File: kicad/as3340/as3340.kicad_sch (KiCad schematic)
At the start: 45 parts, among them J1 Conn_01x01, J3 Conn_02x20_Odd_Even, U1 TL074, U11 LM393, U12 TL074, U15 M24C02-WMN, U2 TL074, U4 PS508, U5 MAX333A, U6 AS3360, U7 PCA9555D, U8 DG442CY+, U9 DG442CY+

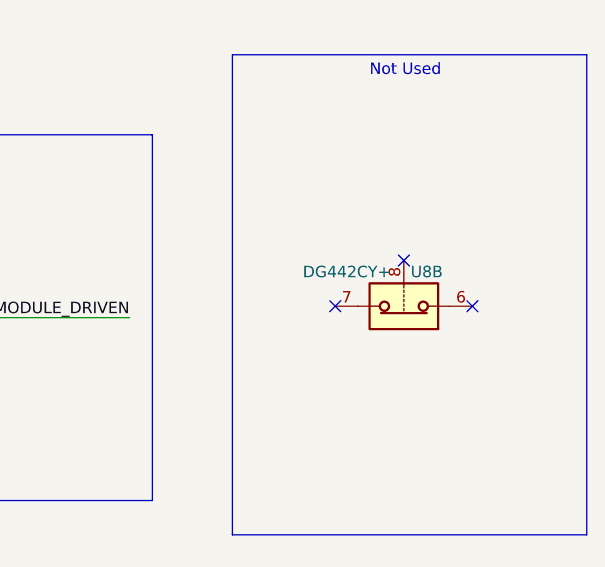
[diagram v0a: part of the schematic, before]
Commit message: tie unused switch to ground
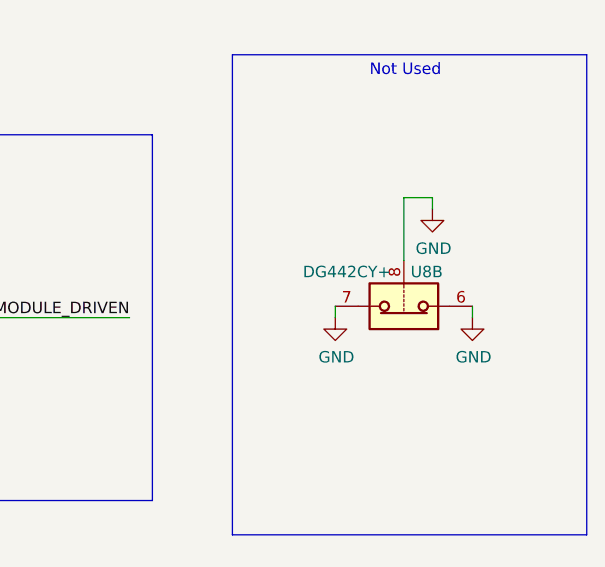
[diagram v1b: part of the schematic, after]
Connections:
- net GND: now also U8.6, U8.7, U8.8
- no-connect marks 12 -> 9
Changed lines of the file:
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@@
   (junction (at 323.85 209.55) (diameter 0) (color 0 0 0 0)
   )
-  (no_connect (at 398.78 203.2))
   (no_connect (at 54.61 77.47))
   (no_connect (at 172.72 54.61))
@@
   (no_connect (at 54.61 34.29))
   (no_connect (at 54.61 72.39))
-  (no_connect (at 406.4 208.28))
-  (no_connect (at 391.16 208.28))
   (no_connect (at 54.61 74.93))
   (wire (pts (xy 24.13 234.95) (xy 24.13 237.49))
@@
     (stroke (width 0) (type default) (color 0 0 0 0))
   )
+  (wire (pts (xy 406.4 208.28) (xy 406.4 209.55))
+    (stroke (width 0) (type default) (color 0 0 0 0))
+  )
   (polyline (pts (xy 293.37 234.95) (xy 293.37 262.89))
     (stroke (width 0) (type default) (color 0 0 0 0))
@@
     (stroke (width 0) (type default) (color 0 0 0 0))
   )
+  (wire (pts (xy 401.955 197.485) (xy 401.955 196.215))
+    (stroke (width 0) (type default) (color 0 0 0 0))
+  )
   (polyline (pts (xy 257.81 262.89) (xy 257.81 234.95))
     (stroke (width 0) (type default) (color 0 0 0 0))
@@
     (stroke (width 0) (type default) (color 0 0 0 0))
   )
+  (wire (pts (xy 391.16 208.28) (xy 391.16 209.55))
+    (stroke (width 0) (type default) (color 0 0 0 0))
+  )
   (wire (pts (xy 109.22 52.07) (xy 109.22 54.61))
     (stroke (width 0) (type default) (color 0 0 0 0))
@@
     (stroke (width 0) (type default) (color 0 0 0 0))
   )
+  (wire (pts (xy 401.955 196.215) (xy 398.78 196.215))
+    (stroke (width 0) (type default) (color 0 0 0 0))
+  )
   (wire (pts (xy 109.22 34.29) (xy 109.22 39.37))
     (stroke (width 0) (type default) (color 0 0 0 0))
@@
     (stroke (width 0) (type default) (color 0 0 0 0))
   )
+  (wire (pts (xy 398.78 196.215) (xy 398.78 203.2))
+    (stroke (width 0) (type default) (color 0 0 0 0))
+  )
   (wire (pts (xy 335.28 52.07) (xy 323.85 52.07))
     (stroke (width 0) (type default) (color 0 0 0 0))
@@
     (pin "1")
   )
+  (symbol (lib_id "power:GND") (at 391.16 209.55 0) (unit 1)
+    (in_bom yes) (on_board yes)
+    (property "Reference" "#PWR071" (id 0) (at 391.16 215.9 0)
+      (effects (font (size 1.27 1.27)) hide)
+    )
+    (property "Value" "GND" (id 1) (at 391.287 213.9442 0))
+    (property "Footprint" "" (id 2) (at 391.16 209.55 0)
+      (effects (font (size 1.27 1.27)) hide)
+    )
+    (property "Datasheet" "" (id 3) (at 391.16 209.55 0)
+      (effects (font (size 1.27 1.27)) hide)
+    )
+    (pin "1")
+  )
+  (symbol (lib_id "power:GND") (at 406.4 209.55 0) (unit 1)
+    (in_bom yes) (on_board yes)
+    (property "Reference" "#PWR074" (id 0) (at 406.4 215.9 0)
+      (effects (font (size 1.27 1.27)) hide)
+    )
+    (property "Value" "GND" (id 1) (at 406.527 213.9442 0))
+    (property "Footprint" "" (id 2) (at 406.4 209.55 0)
+      (effects (font (size 1.27 1.27)) hide)
+    )
+    (property "Datasheet" "" (id 3) (at 406.4 209.55 0)
+      (effects (font (size 1.27 1.27)) hide)
+    )
+    (pin "1")
+  )
   (symbol (lib_id "Connector_Generic:Conn_01x01") (at 391.795 28.575 90) (unit 1)
     (in_bom yes) (on_board yes) (fields_autoplaced)
@@
     (pin "1")
   )
+  (symbol (lib_id "power:GND") (at 401.955 197.485 0) (unit 1)
+    (in_bom yes) (on_board yes)
+    (property "Reference" "#PWR072" (id 0) (at 401.955 203.835 0)
+      (effects (font (size 1.27 1.27)) hide)
+    )
+    (property "Value" "GND" (id 1) (at 402.082 201.8792 0))
+    (property "Footprint" "" (id 2) (at 401.955 197.485 0)
+      (effects (font (size 1.27 1.27)) hide)
+    )
+    (property "Datasheet" "" (id 3) (at 401.955 197.485 0)
+      (effects (font (size 1.27 1.27)) hide)
+    )
+    (pin "1")
+  )
   (sheet (at 162.56 124.46) (size 49.53 45.72) (fields_autoplaced)
     (stroke (width 0) (type solid) (color 0 0 0 0))
@@
       (reference "#PWR070") (unit 1) (value "GND") (footprint "")
     )
+    (path "/2b8704e2-aa1f-40c9-82c8-93dd49fc38ee"
+      (reference "#PWR071") (unit 1) (value "GND") (footprint "")
+    )
+    (path "/ffd638dd-eb53-4da1-84f0-6a181aff412d"
+      (reference "#PWR072") (unit 1) (value "GND") (footprint "")
+    )
     (path "/00000000-0000-0000-0000-000064b423a8"
       (reference "#PWR073") (unit 1) (value "GND") (footprint "")
     )
+    (path "/2e02bdbd-8922-492a-83ea-736cc68f050d"
+      (reference "#PWR074") (unit 1) (value "GND") (footprint "")
+    )
     (path "/00000000-0000-0000-0000-0000645cbcd1"

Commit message: fixes for BOM
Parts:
- C1, C2, C3, C30, C31, C4: LCSC C14663 -> (none)
- U2: LCSC C504548 -> (none)
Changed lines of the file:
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@@
       (effects (font (size 1.27 1.27)) hide)
     )
-    (property "LCSC" "C504548" (id 4) (at 92.71 232.41 0)
+    (property "LCSC" "" (id 4) (at 92.71 232.41 0)
       (effects (font (size 1.27 1.27)) hide)
     )
@@
       (effects (font (size 1.27 1.27)) hide)
     )
-    (property "LCSC" "C14663" (id 4) (at 24.13 241.3 0)
+    (property "LCSC" "" (id 4) (at 24.13 241.3 0)
       (effects (font (size 1.27 1.27)) hide)
     )
@@
       (effects (font (size 1.27 1.27)) hide)
     )
-    (property "LCSC" "C14663" (id 4) (at 24.13 229.87 0)
+    (property "LCSC" "" (id 4) (at 24.13 229.87 0)
       (effects (font (size 1.27 1.27)) hide)
     )
@@
       (effects (font (size 1.27 1.27)) hide)
     )
-    (property "LCSC" "C14663" (id 4) (at 80.01 240.03 0)
-      (effects (font (size 1.27 1.27)) hide)
-    )
     (property "LCSC Part" "C14663" (id 5) (at 80.01 240.03 0)
       (effects (font (size 1.27 1.27)) hide)
@@
     )
     (property "Datasheet" "~" (id 3) (at 80.01 228.6 0)
-      (effects (font (size 1.27 1.27)) hide)
-    )
-    (property "LCSC" "C14663" (id 4) (at 80.01 228.6 0)
       (effects (font (size 1.27 1.27)) hide)
     )
@@
       (effects (font (size 1.27 1.27)) hide)
     )
-    (property "LCSC" "C14663" (id 4) (at 50.8 242.57 0)
-      (effects (font (size 1.27 1.27)) hide)
-    )
     (property "LCSC Part" "C14663" (id 5) (at 50.8 242.57 0)
       (effects (font (size 1.27 1.27)) hide)
@@
       (effects (font (size 1.27 1.27)) hide)
     )
-    (property "LCSC" "C14663" (id 4) (at 50.8 231.14 0)
-      (effects (font (size 1.27 1.27)) hide)
-    )

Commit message: update title block and add schematic pdf
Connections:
- net CARD2_OUT2: no longer names the net of J3.25 (Pin_25)
- net CARD3_OUT2: no longer names the net of J3.27 (Pin_27)
- net CARD4_OUT2: no longer names the net of J3.30 (Pin_30)
- net CARD5_OUT2: no longer names the net of J3.33 (Pin_33)
- net CARD6_OUT2: no longer names the net of J3.35 (Pin_35)
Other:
- title: Zoxnoxious 3340 Oscillator: Top Level -> Zoxnoxious 3340 Oscillator
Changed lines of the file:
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@@
   (paper "B")
   (title_block
-    (title "Zoxnoxious 3340 Oscillator: Top Level")
-    (rev "0.3")
+    (title "Zoxnoxious 3340 Oscillator")
+    (date "2022-09-07")
+    (rev "0.4")
     (company "Zoxnoxious Engineering")
   )
@@
   (junction (at 323.85 209.55) (diameter 0) (color 0 0 0 0)
   )
-  (no_connect (at 54.61 77.47))
+  (no_connect (at 69.85 74.93))
   (no_connect (at 172.72 54.61))
-  (no_connect (at 54.61 69.85))
   (no_connect (at 97.79 36.83))
   (no_connect (at 199.39 82.55))
-  (no_connect (at 97.79 72.39))
   (no_connect (at 54.61 34.29))
-  (no_connect (at 54.61 72.39))
-  (no_connect (at 54.61 74.93))
+  (no_connect (at 69.85 72.39))
+  (no_connect (at 82.55 67.31))
+  (no_connect (at 69.85 64.77))
+  (no_connect (at 69.85 62.23))
   (wire (pts (xy 24.13 234.95) (xy 24.13 237.49))
     (stroke (width 0) (type default) (color 0 0 0 0))
@@
     (stroke (width 0) (type default) (color 0 0 0 0))
   )
-  (wire (pts (xy 69.85 72.39) (xy 54.61 72.39))
-    (stroke (width 0) (type default) (color 0 0 0 0))
-  )
   (polyline (pts (xy 257.81 234.95) (xy 293.37 234.95))
     (stroke (width 0) (type default) (color 0 0 0 0))
@@
     (stroke (width 0) (type default) (color 0 0 0 0))
   )
-  (wire (pts (xy 69.85 74.93) (xy 54.61 74.93))
-    (stroke (width 0) (type default) (color 0 0 0 0))
-  )
   (wire (pts (xy 227.33 246.38) (xy 227.33 248.92))
     (stroke (width 0) (type default) (color 0 0 0 0))
@@
     (stroke (width 0) (type default) (color 0 0 0 0))
   )
-  (wire (pts (xy 54.61 64.77) (xy 69.85 64.77))
-    (stroke (width 0) (type default) (color 0 0 0 0))
-  )
   (wire (pts (xy 90.17 251.46) (xy 80.01 251.46))
     (stroke (width 0) (type default) (color 0 0 0 0))
@@
     (stroke (width 0) (type default) (color 0 0 0 0))
   )
-  (wire (pts (xy 97.79 67.31) (xy 82.55 67.31))
-    (stroke (width 0) (type default) (color 0 0 0 0))
-  )
   (wire (pts (xy 33.02 139.7) (xy 21.59 139.7))
     (stroke (width 0) (type default) (color 0 0 0 0))
@@
   )
   (wire (pts (xy 120.65 157.48) (xy 123.19 157.48))
-    (stroke (width 0) (type default) (color 0 0 0 0))
-  )
-  (wire (pts (xy 54.61 62.23) (xy 69.85 62.23))
     (stroke (width 0) (type default) (color 0 0 0 0))
   )
@@
     (effects (font (size 1.27 1.27)) (justify left bottom))
   )
-  (label "CARD3_OUT2" (at 68.58 64.77 180)
-    (effects (font (size 1.27 1.27)) (justify right bottom))
-  )
   (label "GPIO_MODULE_DRIVEN" (at 368.3 209.55 180)
     (effects (font (size 1.27 1.27)) (justify right bottom))
@@
     (effects (font (size 1.27 1.27)) (justify left bottom))
   )
-  (label "CARD2_OUT2" (at 57.15 62.23 0)
-    (effects (font (size 1.27 1.27)) (justify left bottom))
-  )
   (label "CARD1_OUT1" (at 289.56 40.64 0)
     (effects (font (size 1.27 1.27)) (justify left bottom))
@@
     (effects (font (size 1.27 1.27)) (justify left bottom))
   )
-  (label "CARD4_OUT2" (at 95.25 67.31 180)
-    (effects (font (size 1.27 1.27)) (justify right bottom))
-  )
   (label "SPI_CLK" (at 21.59 135.89 0)
     (effects (font (size 1.27 1.27)) (justify left bottom))
@@
     (effects (font (size 1.27 1.27)) (justify left bottom))
   )
-  (label "CARD6_OUT2" (at 68.58 74.93 180)
-    (effects (font (size 1.27 1.27)) (justify right bottom))
-  )
   (label "SYNC_POS_CTRL" (at 199.39 62.23 0)
     (effects (font (size 1.27 1.27)) (justify left bottom))
@@
     (effects (font (size 1.27 1.27)) (justify left bottom))
   )
-  (label "CARD5_OUT2" (at 67.31 72.39 180)
-    (effects (font (size 1.27 1.27)) (justify right bottom))
-  )
   (label "CARD5_OUT1" (at 67.31 69.85 180)

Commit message: add 3340 v0.4 gerbers
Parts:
- U1, U12, U2: LCSC Part C12594 -> C6963
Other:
- note added: "TL074: LCSC Part C6963 or C12594 works"
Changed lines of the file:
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@@
+    (effects (font (size 1.27 1.27)) (justify left bottom))
+  )
+  (text "TL074: LCSC Part C6963 or C12594 works" (at 27.94 264.16 0)
     (effects (font (size 1.27 1.27)) (justify left bottom))
   )
@@
       (effects (font (size 1.27 1.27)) hide)
     )
-    (property "LCSC Part" "C12594" (id 5) (at 92.71 232.41 0)
+    (property "LCSC Part" "C6963" (id 5) (at 92.71 232.41 0)
       (effects (font (size 1.27 1.27)) hide)
     )
@@
       (effects (font (size 1.27 1.27)) hide)
     )
-    (property "LCSC Part" "C12594" (id 4) (at 314.96 209.55 0)
+    (property "LCSC Part" "C6963" (id 4) (at 314.96 209.55 0)
       (effects (font (size 1.27 1.27)) hide)
     )
@@
       (effects (font (size 1.27 1.27)) hide)
     )
-    (property "LCSC Part" "C12594" (id 5) (at 36.83 233.68 0)
+    (property "LCSC Part" "C6963" (id 5) (at 36.83 233.68 0)
       (effects (font (size 1.27 1.27)) hide)
     )
@@
       (effects (font (size 1.27 1.27)) hide)
     )
-    (property "LCSC Part" "C12594" (id 5) (at 63.5 234.95 0)
-      (effects (font (size 1.27 1.27)) hide)
-    )
+    (property "LCSC Part" "C6963" (id 5) (at 63.5 234.95 0)
+      (effects (font (size 1.27 1.27)) hide)
+    )

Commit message: as3340 rev0.4 submitted to jlcpcb
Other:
- note added: "GND Test Point"
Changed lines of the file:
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@@
+    (stroke (width 0) (type default) (color 0 0 0 0))
+  )
+  (polyline (pts (xy 407.67 21.59) (xy 407.67 45.72))
     (stroke (width 0) (type default) (color 0 0 0 0))
   )
@@
     (stroke (width 0) (type default) (color 0 0 0 0))
   )
+  (polyline (pts (xy 382.27 21.59) (xy 407.67 21.59))
+    (stroke (width 0) (type default) (color 0 0 0 0))
+  )
   (wire (pts (xy 276.86 30.48) (xy 276.86 35.56))
     (stroke (width 0) (type default) (color 0 0 0 0))
@@
     (stroke (width 0) (type default) (color 0 0 0 0))
   )
+  (polyline (pts (xy 382.27 21.59) (xy 382.27 45.72))
+    (stroke (width 0) (type default) (color 0 0 0 0))
+  )
   (wire (pts (xy 82.55 34.29) (xy 109.22 34.29))
     (stroke (width 0) (type default) (color 0 0 0 0))
@@
   )
   (wire (pts (xy 336.55 204.47) (xy 336.55 209.55))
+    (stroke (width 0) (type default) (color 0 0 0 0))
+  )
+  (polyline (pts (xy 407.67 45.72) (xy 382.27 45.72))
     (stroke (width 0) (type default) (color 0 0 0 0))
   )
@@
     (effects (font (size 1.27 1.27)) (justify left bottom))
   )
+  (text "GND Test Point" (at 386.08 25.4 0)
+    (effects (font (size 1.27 1.27)) (justify left bottom))
+  )

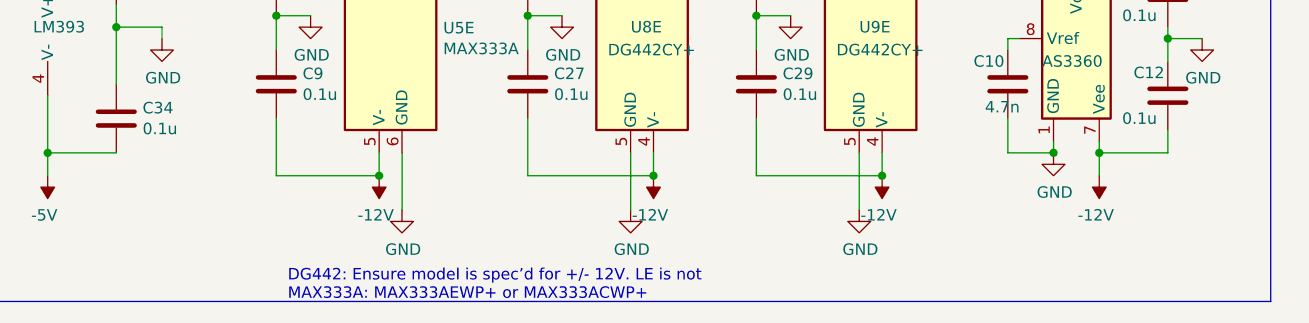
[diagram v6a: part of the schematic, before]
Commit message: update schematic comment on part 333A
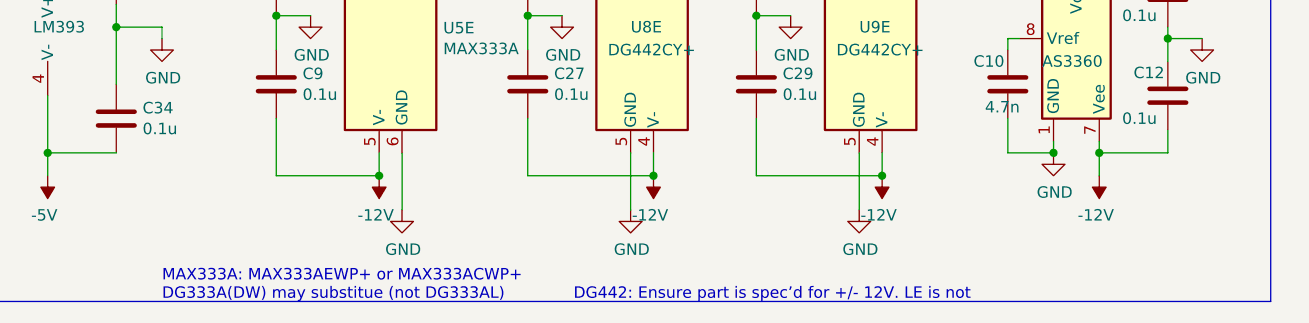
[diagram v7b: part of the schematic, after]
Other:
- note added: "DG442: Ensure part is spec’d for +/- 12V. LE is not"
- note added: "MAX333A: MAX333AEWP+ or MAX333ACWP+ DG333A(DW) may substitue (not DG333AL)"
- note removed: "DG442: Ensure model is spec’d for +/- 12V. LE is not MAX333A: MAX333AEWP+ or MAX333ACWP+"
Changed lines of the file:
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@@
     (effects (font (size 1.27 1.27)) (justify left bottom))
   )
-  (text "DG442: Ensure model is spec’d for +/- 12V. LE is not\nMAX333A: MAX333AEWP+ or MAX333ACWP+"
-    (at 129.54 265.43 0)
+  (text "MAX333A: MAX333AEWP+ or MAX333ACWP+\nDG333A(DW) may substitue (not DG333AL)"
+    (at 115.57 265.43 0)
     (effects (font (size 1.27 1.27)) (justify left bottom))
   )
+  (text "DG442: Ensure part is spec’d for +/- 12V. LE is not"
+    (at 161.29 265.43 0)
+    (effects (font (size 1.27 1.27)) (justify left bottom))
+  )

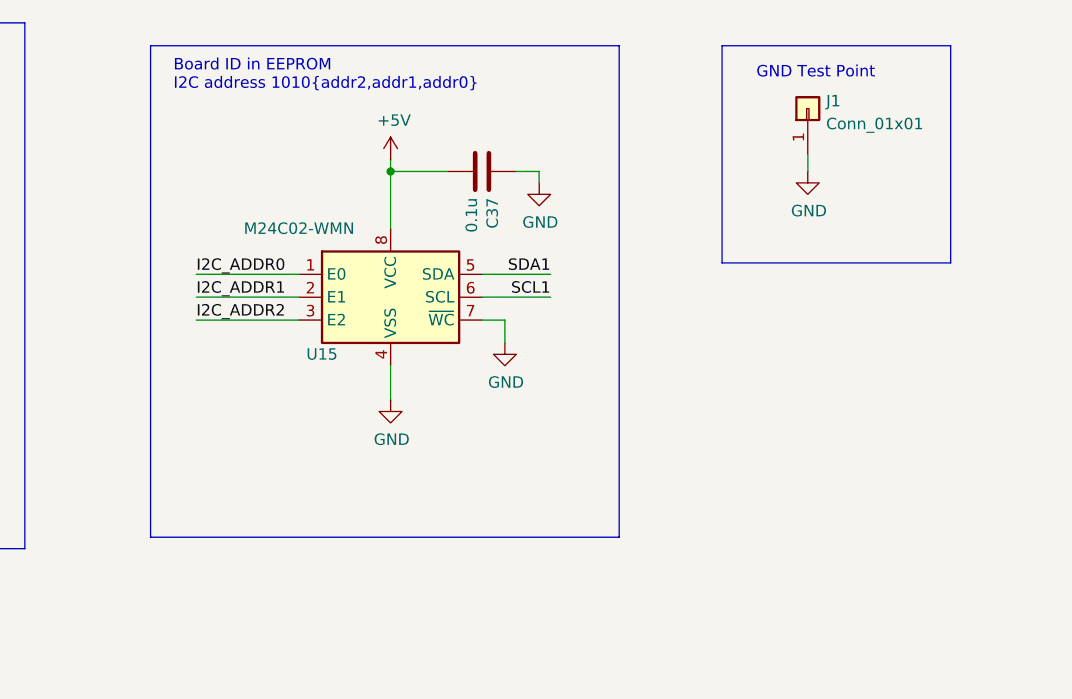
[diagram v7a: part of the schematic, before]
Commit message: starting updates for v0.5
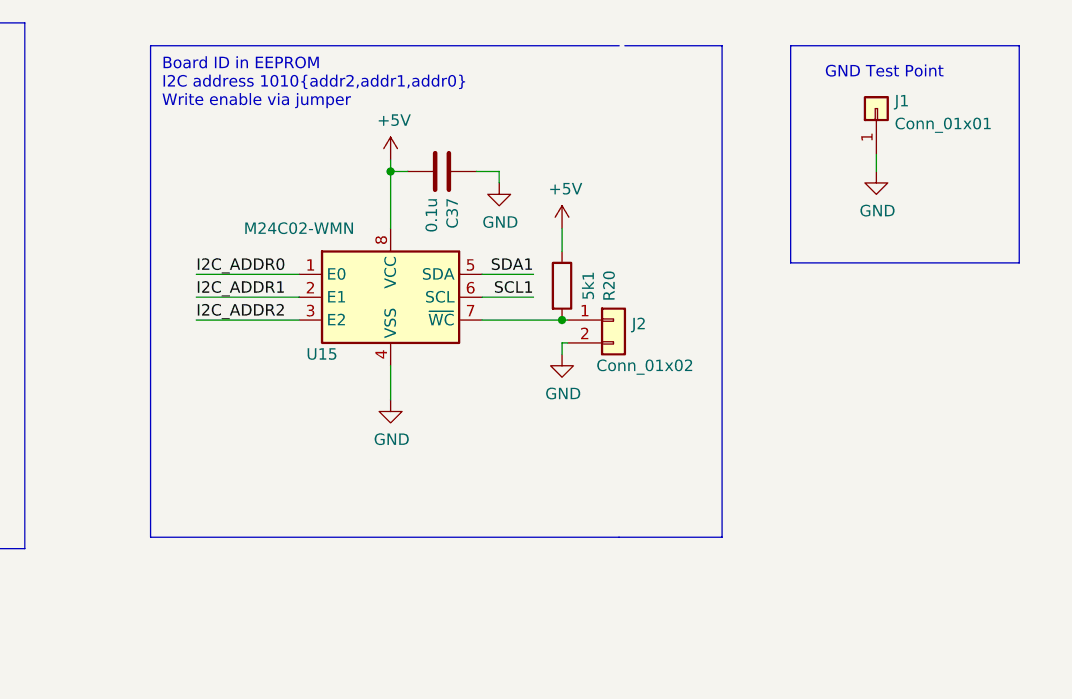
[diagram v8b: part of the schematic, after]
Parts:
- added J2: Conn_01x02, Connector_PinHeader_2.54mm:PinHeader_1x02_P2.54mm_Vertical, symbol Connector_Generic:Conn_01x02
- added R20: 5k1, Resistor_SMD:R_0603_1608Metric, symbol Device:R
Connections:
- net +5V: now also R20.1
- net GND: now also J2.2 (Pin_2); no longer U15.7 (~{WC})
- new net: J2.1 (Pin_1), R20.2, U15.7 (~{WC})
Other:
- note added: "Board ID in EEPROM I2C address 1010{addr2,addr1,addr0} Write enable via jumper"
- note removed: "Board ID in EEPROM I2C address 1010{addr2,addr1,addr0}"
- moved on the sheet: C37, J1
